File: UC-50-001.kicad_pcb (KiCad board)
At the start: 2 copper layers, 283 x 177.5 mm, 255 parts, among them J01 Jumper Wire, J02 Jumper Wire, J03 Jumper wire, J04 Jumper wire, J05 Jumper Wire, J07 Jumper wire, P01 1K, P02 ?, Q01 16MHz, T01 BC547B, T02 BC547B, T03 BC547B, T04 BC557B, T05 BC547B, T06 BC547B, T07 BC547B, T08 BC557B, T09 BC547B, T10 BC547B, T11 BC547B, T12 BDX54, T13 BC547B

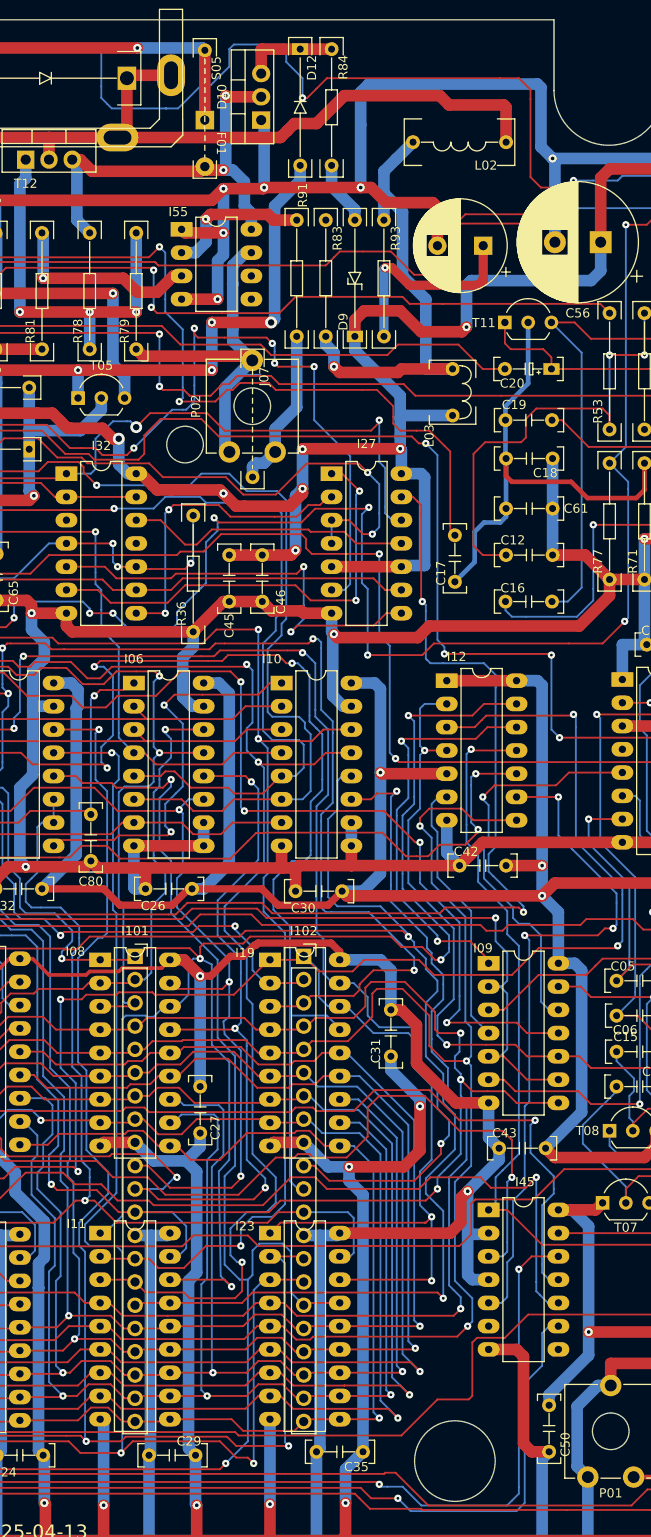
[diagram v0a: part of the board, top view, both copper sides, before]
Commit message: [pcb] silkscreen, area E.*
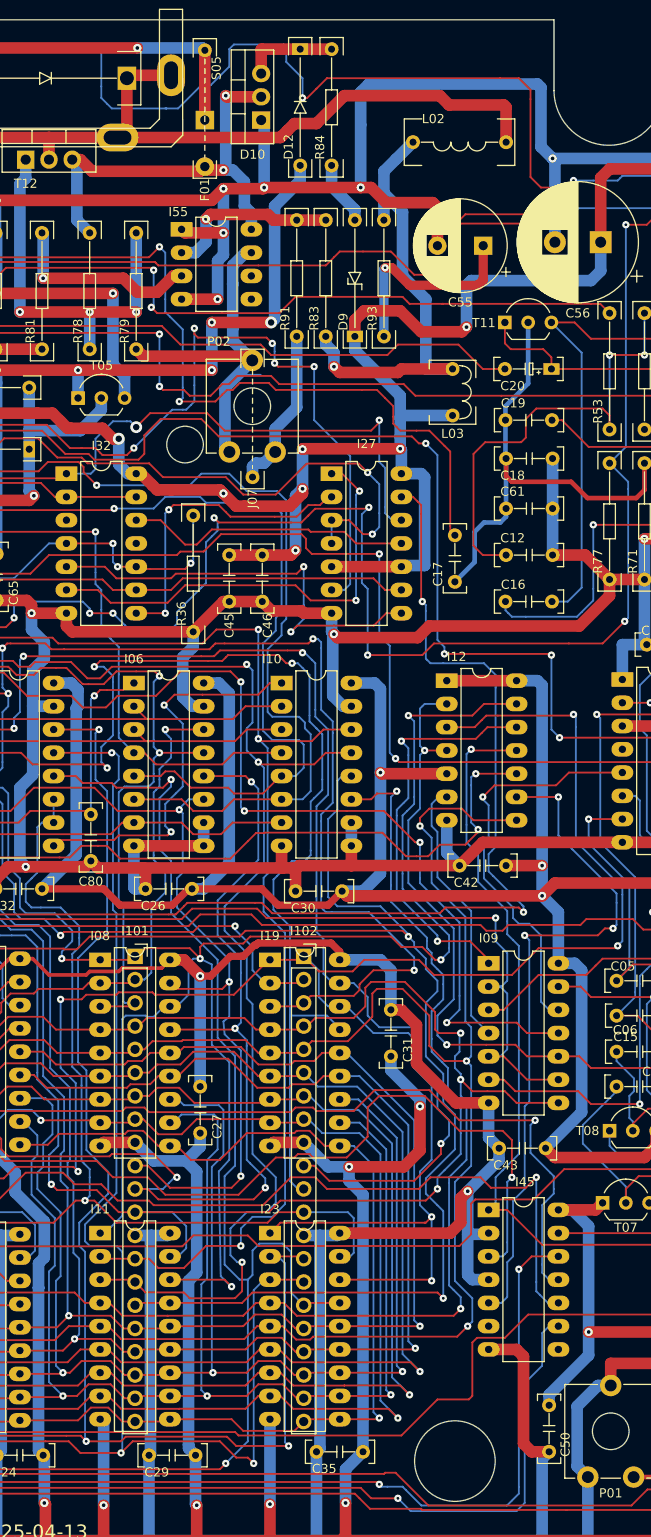
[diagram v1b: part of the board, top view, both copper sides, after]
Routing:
- net Net-(I55-IN+): track 16.0 -> 19.2 mm
